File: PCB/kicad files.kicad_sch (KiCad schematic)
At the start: 0 parts

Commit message: microcotroler schema
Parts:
- added SW1, SW2, SW3: SW_Push, symbol Switch:SW_Push
- added U1: MOUDLE-SEEEDUINO-XIAO, symbol XIAO_RP2040:MOUDLE-SEEEDUINO-XIAO
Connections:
- new net: SW3.1, U1.9 (PA7_A8_D8_SCK)
- new net: SW1.1, U1.11 (PA6_A10_D10_MOSI)
- new net: SW2.1, U1.10 (PA5_A9_D9_MISO)
- new net GND: SW1.2, SW2.2, SW3.2, U1.13 (GND)

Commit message: switch and diode schema
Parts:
- removed SW1, SW2, SW3: SW_Push, symbol Switch:SW_Push
- added D1, D2, D3, D4, D5, D6, D7, D8, D9: D, symbol Device:D
- added SW1, SW2, SW3, SW4, SW5, SW6, SW7, SW8, SW9: SW_Push_45deg, symbol Switch:SW_Push_45deg
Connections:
- net GND: no longer names the net of U1.13 (GND)
- new net: D2.2 (A), SW2.2
- new net: D5.2 (A), SW5.2
- new net: D1.2 (A), SW1.2
- new net: D4.2 (A), SW4.2
- new net: D8.2 (A), SW8.2
- new net: D9.2 (A), SW9.2
- new net: D3.2 (A), SW3.2
- new net: D6.2 (A), SW6.2
- new net: D7.2 (A), SW7.2
- new net Row 0: D1.1 (K), D2.1 (K), D3.1 (K), D4.1 (K), D5.1 (K), D6.1 (K), D7.1 (K), D8.1 (K), D9.1 (K)
- new net column 0: SW1.1, SW4.1, SW7.1
- new net column 1: SW2.1, SW5.1, SW8.1
- new net column 2: SW3.1, SW6.1, SW9.1
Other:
- moved on the sheet: U1

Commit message: schematic done yaaaay
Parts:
- removed U1: MOUDLE-SEEEDUINO-XIAO, symbol XIAO_RP2040:MOUDLE-SEEEDUINO-XIAO
- added D10, D11, D12, D13, D14, D15, D16, D17, D18, D19, D20, D21, D22, D23: SK6812MINI, LED_SMD:LED_SK6812MINI_PLCC4_3.5x3.5mm_P1.75mm, symbol LED:SK6812MINI
- added J2: Conn_01x04_Pin, symbol Connector:Conn_01x04_Pin
- added SW10: RotaryEncoder_Switch, symbol Device:RotaryEncoder_Switch
- added U1: XIAO-RP2040-DIP, Seeed Studio XIAO Series Library:XIAO-RP2040-DIP, symbol Seeed_Studio_XIAO_Series:XIAO-RP2040-DIP
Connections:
- net Row 0: now also U1.3 (GPIO28/ADC2/A2); no longer D4.1 (K), D5.1 (K), D6.1 (K), D7.1 (K), D8.1 (K), D9.1 (K)
- new net: D21.1 (DOUT), D22.3 (DIN)
- new net: D20.1 (DOUT), D21.3 (DIN)
- new net: D19.1 (DOUT), D20.3 (DIN)
- new net: D12.1 (DOUT), D13.3 (DIN)
- new net: D11.1 (DOUT), D12.3 (DIN)
- new net: D18.1 (DOUT), D19.3 (DIN)
- new net: D17.1 (DOUT), D18.3 (DIN)
- new net: D16.1 (DOUT), D17.3 (DIN)
- new net: D22.1 (DOUT), D23.3 (DIN)
- new net: D10.1 (DOUT), D11.3 (DIN)
- new net: D14.1 (DOUT), D15.3 (DIN)
- new net: D13.1 (DOUT), D14.3 (DIN)
- new net: D15.1 (DOUT), D16.3 (DIN)
- new net +3.3V: U1.12 (3V3)
- new net +5V: D10.4 (VDD), D11.4 (VDD), D12.4 (VDD), D13.4 (VDD), D14.4 (VDD), D15.4 (VDD), D16.4 (VDD), D17.4 (VDD), D18.4 (VDD), D19.4 (VDD), D20.4 (VDD), D21.4 (VDD), D22.4 (VDD), D23.4 (VDD), J2.2 (Pin_2), U1.14 (VBUS)
- new net Column 0: U1.11 (GPIO3/MOSI)
- new net Column 1: U1.10 (GPIO4/MISO)
- new net Column 2: U1.9 (GPIO2/SCK)
- new net ENC_A: SW10.A, U1.1 (GPIO26/ADC0/A0)
- new net ENC_B: SW10.B, U1.2 (GPIO27/ADC1/A1)
- new net GND: D10.2 (VSS), D11.2 (VSS), D12.2 (VSS), D13.2 (VSS), D14.2 (VSS), D15.2 (VSS), D16.2 (VSS), D17.2 (VSS), D18.2 (VSS), D19.2 (VSS), D20.2 (VSS), D21.2 (VSS), D22.2 (VSS), D23.2 (VSS), J2.1 (Pin_1), SW10.C, SW10.S1, U1.13 (GND)
- new net LED Data: D10.3 (DIN), U1.8 (GPIO1/RX)
- new net Row 1: D4.1 (K), D5.1 (K), D6.1 (K), U1.4 (GPIO29/ADC3/A3)
- new net Row 2: D7.1 (K), D8.1 (K), D9.1 (K), U1.7 (GPIO0/TX)
- new net SCL: J2.3 (Pin_3), U1.6 (GPIO7/SCL)
- new net SDA: J2.4 (Pin_4), U1.5 (GPIO6/SDA)
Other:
- moved on the sheet: D1, D2, D3, D4, D5, D6, D7, D8, D9, SW1, SW2, SW3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

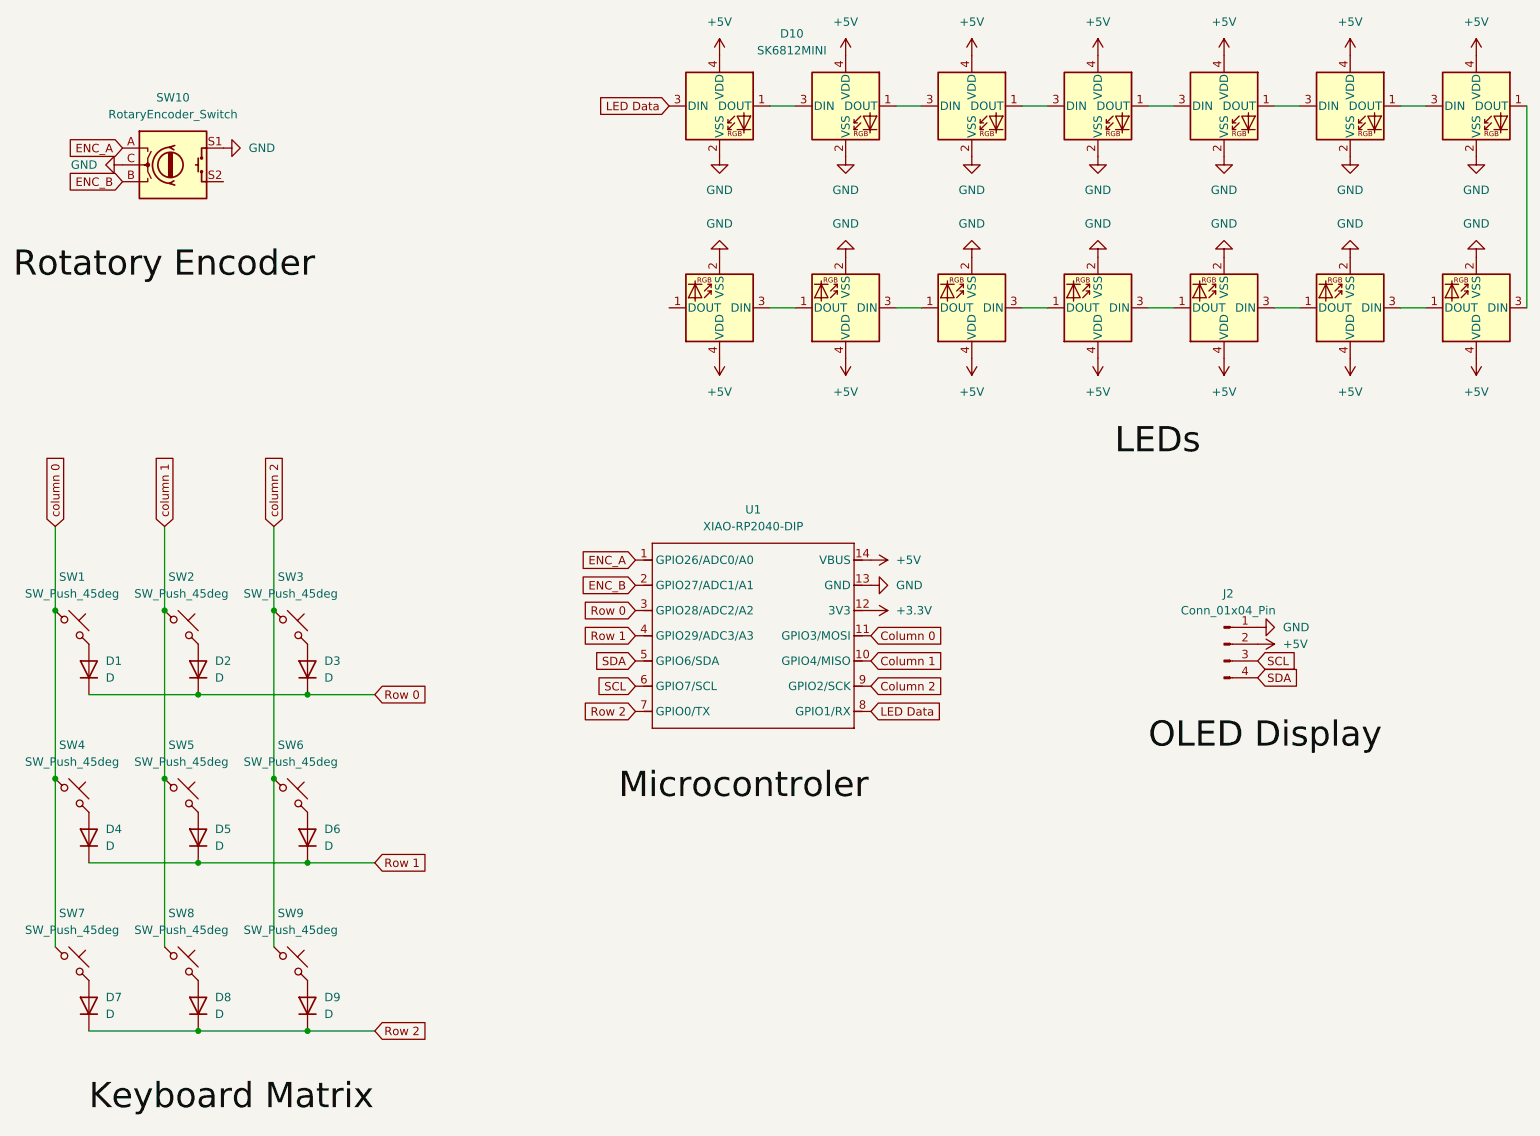
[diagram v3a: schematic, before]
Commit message: assigned footprints
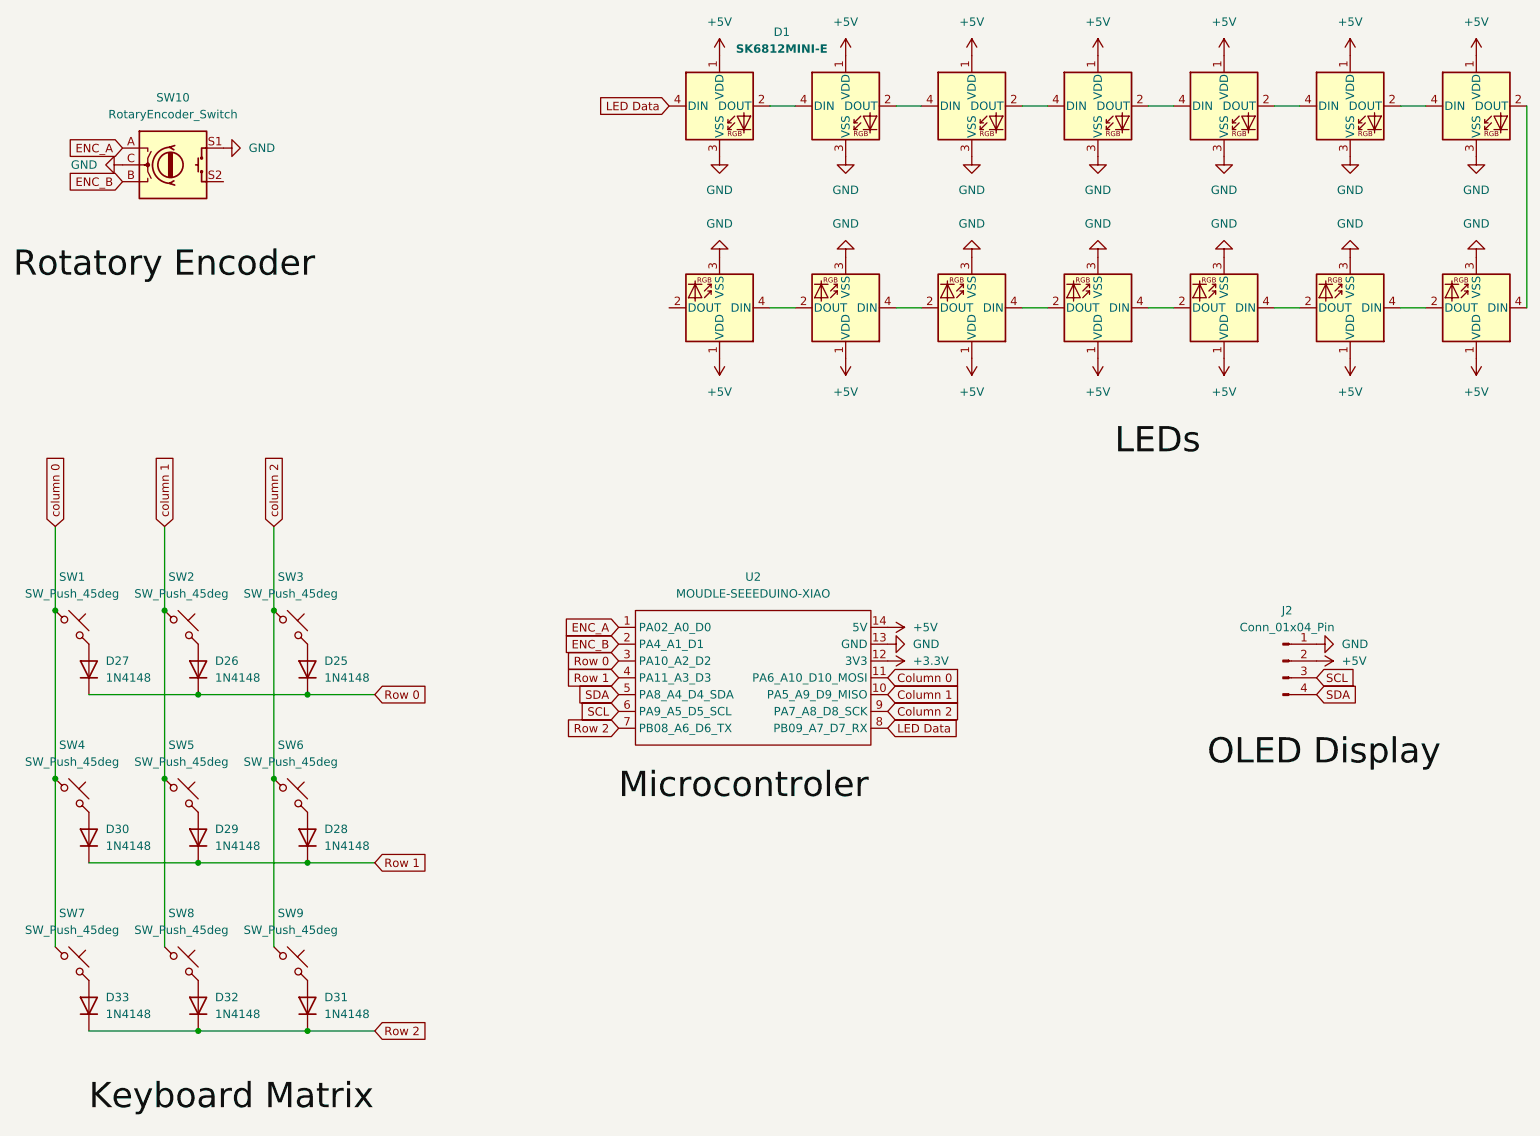
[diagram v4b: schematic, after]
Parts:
- removed D1, D2, D3, D4, D5, D6, D7, D8, D9: D, symbol Device:D
- removed D10, D11, D12, D13, D14, D15, D16, D17, D18, D19, D20, D21, D22, D23: SK6812MINI, LED_SMD:LED_SK6812MINI_PLCC4_3.5x3.5mm_P1.75mm, symbol LED:SK6812MINI
- removed U1: XIAO-RP2040-DIP, Seeed Studio XIAO Series Library:XIAO-RP2040-DIP, symbol Seeed_Studio_XIAO_Series:XIAO-RP2040-DIP
- added D1, D10, D11, D12, D13, D14, D15, D3, D4, D5, D6, D7, D8, D9: SK6812MINI-E, footprints:SK6812MINI-E_fixed, symbol SK6812MINI-E:SK6812MINI-E
- added D25, D26, D27, D28, D29, D30, D31, D32, D33: 1N4148, Diode_THT:D_DO-35_SOD27_P7.62mm_Horizontal, symbol Diode:1N4148
- added U2: MOUDLE-SEEEDUINO-XIAO, footprints:XIAO-Generic-Hybrid-14P-2.54-21X17.8MM, symbol XIAO_RP2040:MOUDLE-SEEEDUINO-XIAO
- J2: footprint (none) -> Connector_PinHeader_2.54mm:PinHeader_1x04_P2.54mm_Vertical
- SW1, SW2, SW3, SW4, SW5, SW6, SW7, SW8, SW9: footprint (none) -> Button_Switch_Keyboard:SW_Cherry_MX_1.00u_PCB
- SW10: footprint (none) -> Rotary_Encoder:RotaryEncoder_Alps_EC11E-Switch_Vertical_H20mm
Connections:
- net +3.3V: now also U2.12 (3V3)
- net +5V: now also D1.1 (VDD), D10.1 (VDD), D11.1 (VDD), D12.1 (VDD), D13.1 (VDD), D14.1 (VDD), D15.1 (VDD), D3.1 (VDD), D4.1 (VDD), D5.1 (VDD), D6.1 (VDD), D7.1 (VDD), D8.1 (VDD), D9.1 (VDD), U2.14 (5V)
- net Column 0: now also U2.11 (PA6_A10_D10_MOSI)
- net Column 1: now also U2.10 (PA5_A9_D9_MISO)
- net Column 2: now also U2.9 (PA7_A8_D8_SCK)
- net ENC_A: now also U2.1 (PA02_A0_D0)
- net ENC_B: now also U2.2 (PA4_A1_D1)
- net GND: now also D1.3 (VSS), D10.3 (VSS), D11.3 (VSS), D12.3 (VSS), D13.3 (VSS), D14.3 (VSS), D15.3 (VSS), D3.3 (VSS), D4.3 (VSS), D5.3 (VSS), D6.3 (VSS), D7.3 (VSS), D8.3 (VSS), D9.3 (VSS), U2.13 (GND)
- net LED Data: now also D1.4 (DIN), U2.8 (PB09_A7_D7_RX)
- net Row 0: now also D25.1 (K), D26.1 (K), D27.1 (K), U2.3 (PA10_A2_D2)
- net Row 1: now also D28.1 (K), D29.1 (K), D30.1 (K), U2.4 (PA11_A3_D3)
- net Row 2: now also D31.1 (K), D32.1 (K), D33.1 (K), U2.7 (PB08_A6_D6_TX)
- net SCL: now also U2.6 (PA9_A5_D5_SCL)
- net SDA: now also U2.5 (PA8_A4_D4_SDA)
- net at SW2.2: now also D26.2 (A)
- net at SW5.2: now also D29.2 (A)
- net at SW1.2: now also D27.2 (A)
- net at SW4.2: now also D30.2 (A)
- net at SW8.2: now also D32.2 (A)
- net at SW9.2: now also D31.2 (A)
- net at SW3.2: now also D25.2 (A)
- net at SW6.2: now also D28.2 (A)
- net at SW7.2: now also D33.2 (A)
- new net: D3.2 (DOUT), D4.4 (DIN)
- new net: D1.2 (DOUT), D3.4 (DIN)
- new net: D6.2 (DOUT), D7.4 (DIN)
- new net: D5.2 (DOUT), D6.4 (DIN)
- new net: D11.2 (DOUT), D12.4 (DIN)
- new net: D10.2 (DOUT), D11.4 (DIN)
- new net: D8.2 (DOUT), D9.4 (DIN)
- new net: D7.2 (DOUT), D8.4 (DIN)
- new net: D10.4 (DIN), D9.2 (DOUT)
- new net: D4.2 (DOUT), D5.4 (DIN)
- new net: D12.2 (DOUT), D13.4 (DIN)
- new net: D14.2 (DOUT), D15.4 (DIN)
- new net: D13.2 (DOUT), D14.4 (DIN)
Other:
- moved on the sheet: J2

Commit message: placed LEDs
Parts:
- renumbered D11 to D10, D7 to D11, D10 to D12, D8 to D13, D9 to D14, D15 to D2, D14 to D4, D4 to D5, D13 to D6, D5 to D7, D12 to D8, D6 to D9
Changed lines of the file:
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@@
 		(dnp no)
 		(fields_autoplaced yes)
-		(property "Reference" "D6"
+		(property "Reference" "D9"
 			(at 240.03 31.6798 0)
 			(hide yes)
@@
 			(project "kicad files"
 				(path "/88ceca4b-52c7-47e0-8744-4f7df2c73c46"
-					(reference "D6")
+					(reference "D9")
 					(unit 1)
 				)
@@
 		(dnp no)
 		(fields_autoplaced yes)
-		(property "Reference" "D11"
+		(property "Reference" "D10"
 			(at 189.23 75.0002 0)
 			(hide yes)
@@
 			(project "kicad files"
 				(path "/88ceca4b-52c7-47e0-8744-4f7df2c73c46"
-					(reference "D11")
+					(reference "D10")
 					(unit 1)
 				)
@@
 		(dnp no)
 		(fields_autoplaced yes)
-		(property "Reference" "D8"
+		(property "Reference" "D13"
 			(at 278.13 31.6798 0)
 			(hide yes)
@@
 			(project "kicad files"
 				(path "/88ceca4b-52c7-47e0-8744-4f7df2c73c46"
-					(reference "D8")
+					(reference "D13")
 					(unit 1)
 				)
@@
 		(dnp no)
 		(fields_autoplaced yes)
-		(property "Reference" "D9"
+		(property "Reference" "D14"
 			(at 227.33 75.0002 0)
 			(hide yes)
@@
 			(project "kicad files"
 				(path "/88ceca4b-52c7-47e0-8744-4f7df2c73c46"
-					(reference "D9")
+					(reference "D14")
 					(unit 1)
 				)
@@
 		(dnp no)
 		(fields_autoplaced yes)
-		(property "Reference" "D10"
+		(property "Reference" "D12"
 			(at 208.28 75.0002 0)
 			(hide yes)
@@
 			(project "kicad files"
 				(path "/88ceca4b-52c7-47e0-8744-4f7df2c73c46"
-					(reference "D10")
+					(reference "D12")
 					(unit 1)
 				)
@@
 		(dnp no)
 		(fields_autoplaced yes)
-		(property "Reference" "D5"
+		(property "Reference" "D7"
 			(at 220.98 31.6798 0)
 			(hide yes)
@@
 			(project "kicad files"
 				(path "/88ceca4b-52c7-47e0-8744-4f7df2c73c46"
-					(reference "D5")
+					(reference "D7")
 					(unit 1)
 				)
@@
 		(dnp no)
 		(fields_autoplaced yes)
-		(property "Reference" "D12"
+		(property "Reference" "D8"
 			(at 170.18 75.0002 0)
 			(hide yes)
@@
 			(project "kicad files"
 				(path "/88ceca4b-52c7-47e0-8744-4f7df2c73c46"
-					(reference "D12")
+					(reference "D8")
 					(unit 1)
 				)
@@
 		(dnp no)
 		(fields_autoplaced yes)
-		(property "Reference" "D4"
+		(property "Reference" "D5"
 			(at 201.93 31.6798 0)
 			(hide yes)
@@
 			(project "kicad files"
 				(path "/88ceca4b-52c7-47e0-8744-4f7df2c73c46"
-					(reference "D4")
+					(reference "D5")
 					(unit 1)
 				)
@@
 		(dnp no)
 		(fields_autoplaced yes)
-		(property "Reference" "D14"
+		(property "Reference" "D4"
 			(at 132.08 75.0002 0)
 			(hide yes)
@@
 			(project "kicad files"
 				(path "/88ceca4b-52c7-47e0-8744-4f7df2c73c46"
-					(reference "D14")
+					(reference "D4")
 					(unit 1)
 				)
@@
 		(dnp no)
 		(fields_autoplaced yes)
-		(property "Reference" "D15"
+		(property "Reference" "D2"
 			(at 113.03 75.0002 0)
 			(hide yes)
@@
 			(project "kicad files"
 				(path "/88ceca4b-52c7-47e0-8744-4f7df2c73c46"
-					(reference "D15")
+					(reference "D2")
 					(unit 1)
 				)
@@
 		(dnp no)
 		(fields_autoplaced yes)
-		(property "Reference" "D7"
+		(property "Reference" "D11"
 			(at 259.08 31.6798 0)
 			(hide yes)
@@
 			(project "kicad files"
 				(path "/88ceca4b-52c7-47e0-8744-4f7df2c73c46"
-					(reference "D7")
+					(reference "D11")
 					(unit 1)
 				)
@@
 		(dnp no)
 		(fields_autoplaced yes)
-		(property "Reference" "D13"
+		(property "Reference" "D6"
 			(at 151.13 75.0002 0)
 			(hide yes)
@@
 			(project "kicad files"
 				(path "/88ceca4b-52c7-47e0-8744-4f7df2c73c46"
-					(reference "D13")
+					(reference "D6")
 					(unit 1)
 				)

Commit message: pcb finally done with 64 fucking errorss
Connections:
- net Column 0 is gone; now on net column 0: U2.11 (PA6_A10_D10_MOSI)
- net Column 1 is gone; now on net column 1: U2.10 (PA5_A9_D9_MISO)
- net Column 2 is gone; now on net column 2: U2.9 (PA7_A8_D8_SCK)
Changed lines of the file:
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@@
 		)
 	)
-	(global_label "Column 1"
+	(global_label "column 1"
 		(shape input)
 		(at 163.83 127 0)
@@
 		)
 		(property "Intersheetrefs" "${INTERSHEET_REFS}"
-			(at 176.0678 127 0)
-			(hide yes)
-			(show_name no)
-			(do_not_autoplace no)
-			(effects
-				(font
-					(size 1.27 1.27)
-				)
-				(justify left)
-			)
-		)
-	)
-	(global_label "Column 0"
+			(at 175.8864 127 0)
+			(hide yes)
+			(show_name no)
+			(do_not_autoplace no)
+			(effects
+				(font
+					(size 1.27 1.27)
+				)
+				(justify left)
+			)
+		)
+	)
+	(global_label "column 0"
 		(shape input)
 		(at 163.83 124.46 0)
@@
 		)
 		(property "Intersheetrefs" "${INTERSHEET_REFS}"
-			(at 176.0678 124.46 0)
+			(at 175.8864 124.46 0)
 			(hide yes)
 			(show_name no)
@@
 		)
 	)
-	(global_label "Column 2"
+	(global_label "column 2"
 		(shape input)
 		(at 163.83 129.54 0)
@@
 		)
 		(property "Intersheetrefs" "${INTERSHEET_REFS}"
-			(at 176.0678 129.54 0)
-			(hide yes)
-			(show_name no)
+			(at 175.8864 129.54 0)
+			(hide yes)
+			(show_name no)
